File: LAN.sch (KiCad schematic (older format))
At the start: 32 parts

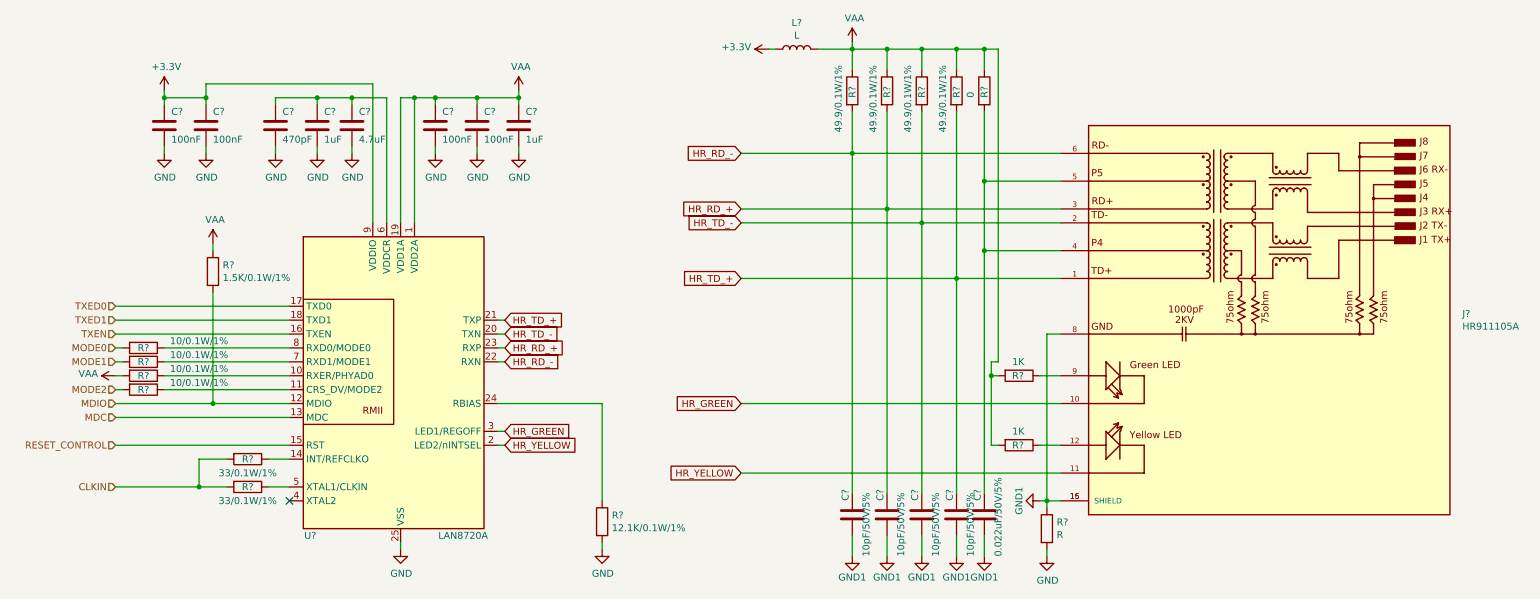
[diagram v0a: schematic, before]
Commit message: Exported first net
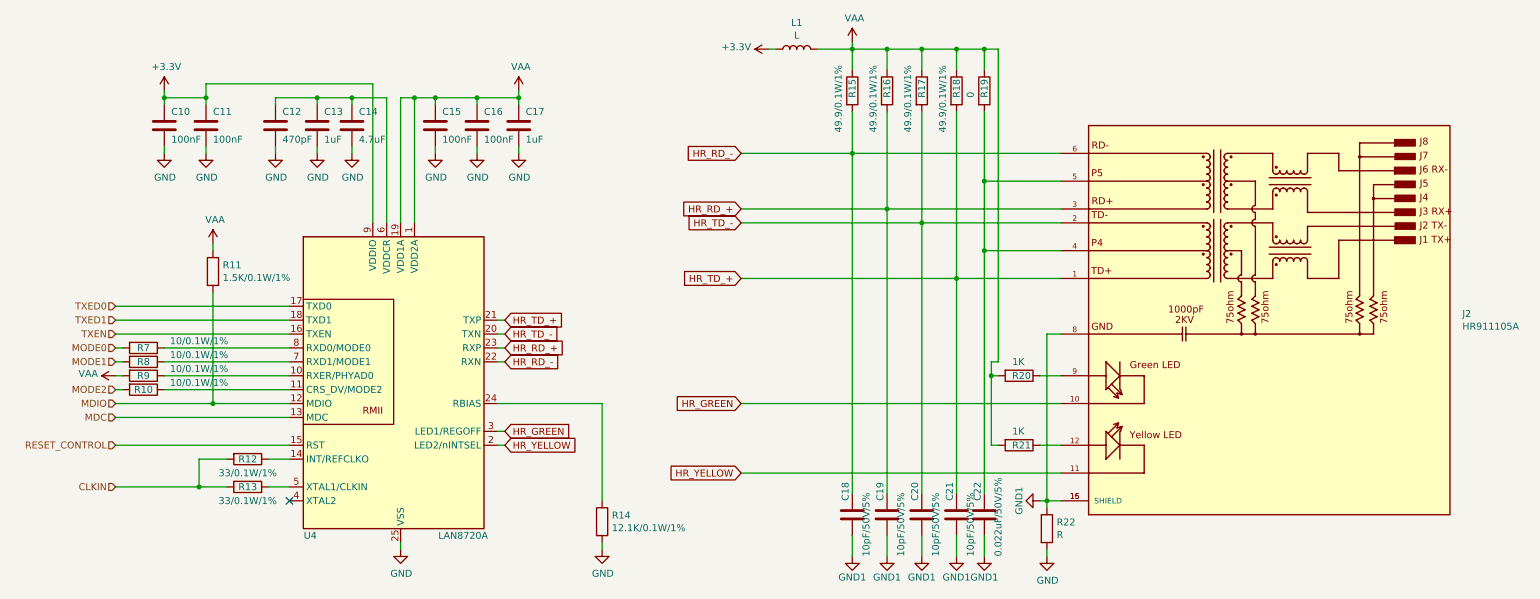
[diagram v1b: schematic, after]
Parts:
- J2: renamed from J?; footprint HANRUN_HR911105A -> expander:HANRUN_HR911105A
- gave numbers to parts that had none: 31

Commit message: Added lcsc part nums
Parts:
- C10, C11, C15, C16: value 100nF -> 100nF/50V/10%; LCSC (none) -> C307331
- C12: value 470pF -> 470pF/50V/20%; LCSC (none) -> C1537
- C13, C17: value 1uF -> 1uF/10%/25V; LCSC (none) -> C52923
- C14: value 4.7uF -> 4.7uF/10V/20%; LCSC (none) -> C23733
- C18, C19, C20, C21: LCSC (none) -> C32949
- C22: LCSC (none) -> C1531
- L1: value L -> PZ1608D121-2R0TF; LCSC (none) -> C42102
- R10, R7, R8, R9: LCSC (none) -> C25077
- R11: LCSC (none) -> C25867
- R12, R13: LCSC (none) -> C25105
- R14: LCSC (none) -> C321280
- R15, R16, R17, R18: LCSC (none) -> C25120
- R19: LCSC (none) -> C17168
- R20, R21: value 1K -> 1K/1/16W/50V; LCSC (none) -> C11702
- R22: LCSC (none) -> C17888
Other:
- moved on the sheet: C12, C13, C14

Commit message: Added bom
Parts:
- J2: LCSC (none) -> C12074; MP HR911105A -> (none); P (none) -> HR911105A
- U4: LCSC (none) -> C45223
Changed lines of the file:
@@
 F 2 "Package_DFN_QFN:QFN-24-1EP_4x4mm_P0.5mm_EP2.6x2.6mm" H 3450 3100 50  0001 L CNN
 F 3 "http://ww1.microchip.com/downloads/en/DeviceDoc/8720a.pdf" H 3200 3200 50  0001 C CNN
+F 4 "C45223" H 3400 4150 50  0001 C CNN "LCSC"
 	1    3400 4150
 	1    0    0    -1
@@
 F 2 "expander:HANRUN_HR911105A" H 9650 3650 50  0001 L BNN
 F 3 "" H 9650 3650 50  0001 L BNN
-F 4 "HR911105A" H 9650 3650 50  0001 L BNN "MP"
+F 4 "HR911105A" H 9650 3650 50  0001 L BNN "P"
 F 5 "None" H 9650 3650 50  0001 L BNN "PACKAGE"
 F 6 "Manufacturer Recommendation" H 9650 3650 50  0001 L BNN "STANDARD"
@@
 F 10 "DIP RJ45 Connector;" H 9650 3650 50  0001 L BNN "DESCRIPTION"
 F 11 "A" H 9650 3650 50  0001 L BNN "PARTREV"
+F 12 "C12074" H 9650 3650 50  0001 C CNN "LCSC"
 	1    9650 3650
 	1    0    0    -1
